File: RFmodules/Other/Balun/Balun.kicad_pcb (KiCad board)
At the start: 2 copper layers, 4 parts, among them J1 SMA, J2 SMA, J3 SMA, U1 T

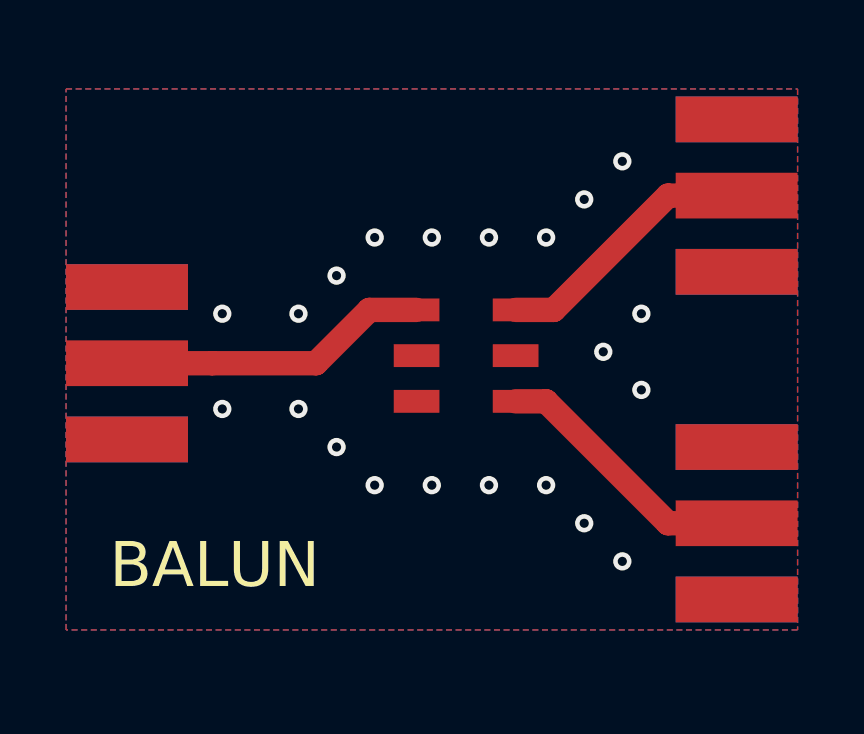
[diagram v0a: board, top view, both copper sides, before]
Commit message: balun footprint clearance chanched
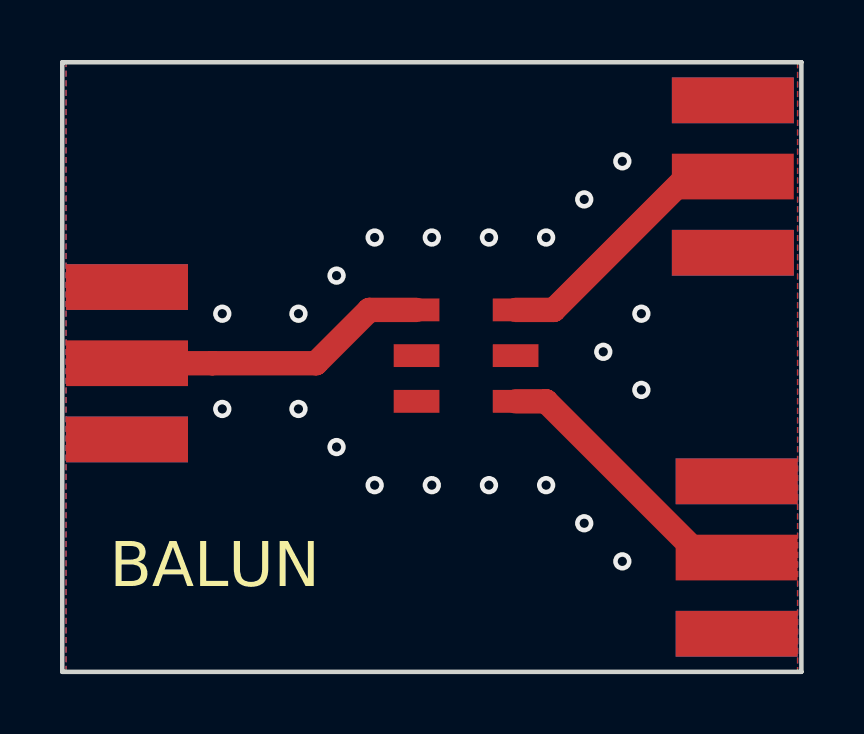
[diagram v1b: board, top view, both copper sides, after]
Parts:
- moved J3 1.14 mm to (88.1, 162.4)
- moved J2 0.65 mm to (88.0, 149.7)
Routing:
- net /out_Px: track 8.94 -> 7.74 mm
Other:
- board outline added: 24.6 x 20.3 mm
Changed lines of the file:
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@@
   (general
     (thickness 1.6)
-    (drawings 1)
+    (drawings 5)
     (tracks 31)
     (zones 0)
@@
   (layers
     (0 F.Cu signal)
-    (31 B.Cu signal)
+    (31 B.Cu signal hide)
     (32 B.Adhes user)
     (33 F.Adhes user)
@@
   )
   (setup
-    (last_trace_width 0.8128)
+    (last_trace_width 0.2032)
     (user_trace_width 0.2032)
     (user_trace_width 0.4064)
@@
   )
   (module RFLego_Footprint:SMA_Edge (layer F.Cu)
-    (at 88.138 150.368)
+    (at 88.011 149.733)
     (fp_text reference J2 (at 2.1336 4.6482) (layer F.SilkS) hide
       (effects (font (size 1 1) (thickness 0.15)))
@@
   )
   (module RFLego_Footprint:SMA_Edge (layer F.Cu)
-    (at 88.138 161.29)
+    (at 88.138 162.433)
     (fp_text reference J3 (at 2.1336 4.6482) (layer F.SilkS) hide
       (effects (font (size 1 1) (thickness 0.15)))
@@
       (net 1 "Net-(J1-Pad1)"))
   )
+  (gr_line (start 67.691 166.243) (end 67.691 145.923) (layer Edge.Cuts) (width 0.15))
+  (gr_line (start 92.329 166.243) (end 67.691 166.243) (layer Edge.Cuts) (width 0.15))
+  (gr_line (start 92.329 145.923) (end 92.329 166.243) (layer Edge.Cuts) (width 0.15))
+  (gr_line (start 67.691 145.923) (end 92.329 145.923) (layer Edge.Cuts) (width 0.15))
   (gr_text BALUN (at 72.771 162.687) (layer F.SilkS)
     (effects (font (size 1.5 1.5) (thickness 0.3)))
@@
   (via (at 80.01 151.765) (size 0.6096) (drill 0.3048) (layers F.Cu B.Cu) (net 2))
   (via (at 81.915 151.765) (size 0.6096) (drill 0.3048) (layers F.Cu B.Cu) (net 2))
-  (segment (start 87.884 161.29) (end 90.17 161.29) (width 0.8128) (layer F.Cu) (net 3))
+  (segment (start 89.027 162.433) (end 90.17 162.433) (width 0.8128) (layer F.Cu) (net 3))
   (segment (start 82.804 157.226) (end 83.82 157.226) (width 0.8128) (layer F.Cu) (net 3))
-  (segment (start 83.82 157.226) (end 87.884 161.29) (width 0.8128) (layer F.Cu) (net 3))
-  (segment (start 87.884 150.368) (end 90.17 150.368) (width 0.8128) (layer F.Cu) (net 4))
+  (segment (start 83.82 157.226) (end 89.027 162.433) (width 0.8128) (layer F.Cu) (net 3))
+  (segment (start 90.043 149.733) (end 90.17 149.86) (width 0.8128) (layer F.Cu) (net 4))
   (segment (start 82.804 154.178) (end 84.074 154.178) (width 0.8128) (layer F.Cu) (net 4))
-  (segment (start 84.074 154.178) (end 87.884 150.368) (width 0.8128) (layer F.Cu) (net 4))
+  (segment (start 84.074 154.178) (end 88.519 149.733) (width 0.8128) (layer F.Cu) (net 4))
   (zone (net 2) (net_name GND) (layer F.Cu) (hatch edge 0.508)
     (connect_pads (clearance 0.508))
@@
     (polygon
       (pts
-        (xy 92.202 146.812) (xy 92.202 164.846) (xy 67.818 164.846) (xy 67.818 146.812)
+        (xy 92.202 145.923) (xy 92.202 166.243) (xy 67.818 166.243) (xy 67.818 145.923)
       )
     )
@@
     (polygon
       (pts
-        (xy 92.202 146.812) (xy 92.202 164.846) (xy 67.818 164.846) (xy 67.818 146.812)
+        (xy 92.202 145.923) (xy 92.202 166.243) (xy 67.818 166.243) (xy 67.818 145.923)
       )
     )
